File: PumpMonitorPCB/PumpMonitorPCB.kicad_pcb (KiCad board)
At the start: 2 copper layers, 51 parts, among them J3 Debug, J4 USB_C_Receptacle_USB2.0_16P, K1 J115F11CH5VDCS61-5U Relay, Q1 AS2302, U1 ACS770xCB-050B-PFF, U2 AMS1117-3.3, U3 ESP32-S3-WROOM-1, U4 MC14504B, U5 WIO-SX1262, U6 TPD3E001DRLR

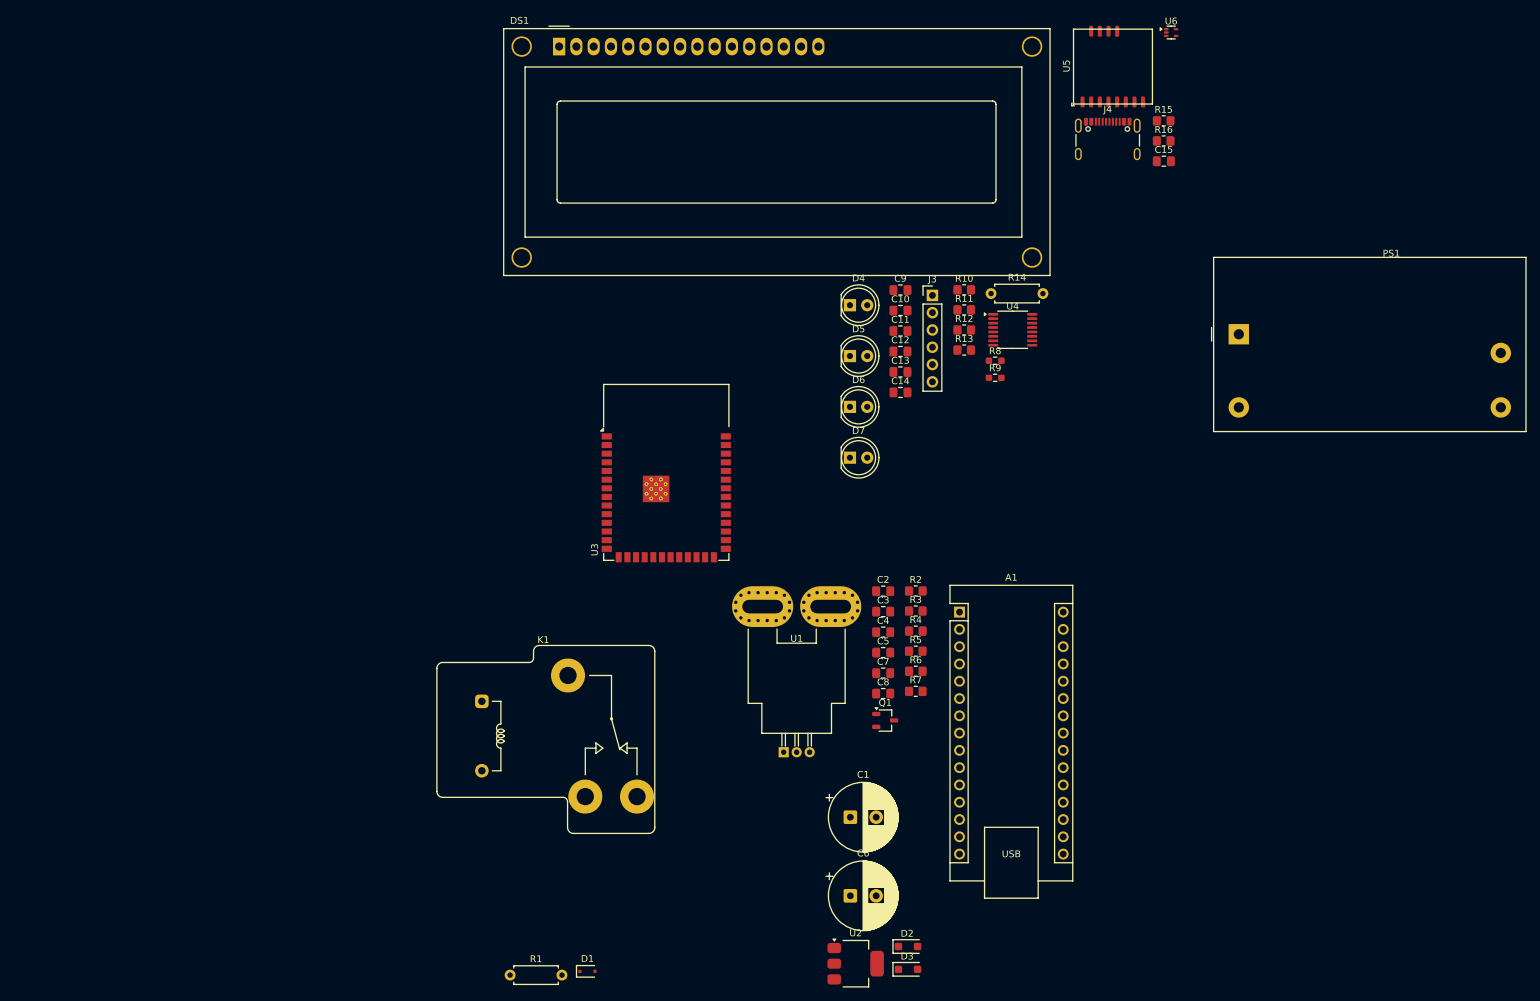
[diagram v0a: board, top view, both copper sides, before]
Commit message: Added op amps to voltage and current measurement, more footprint assignments.
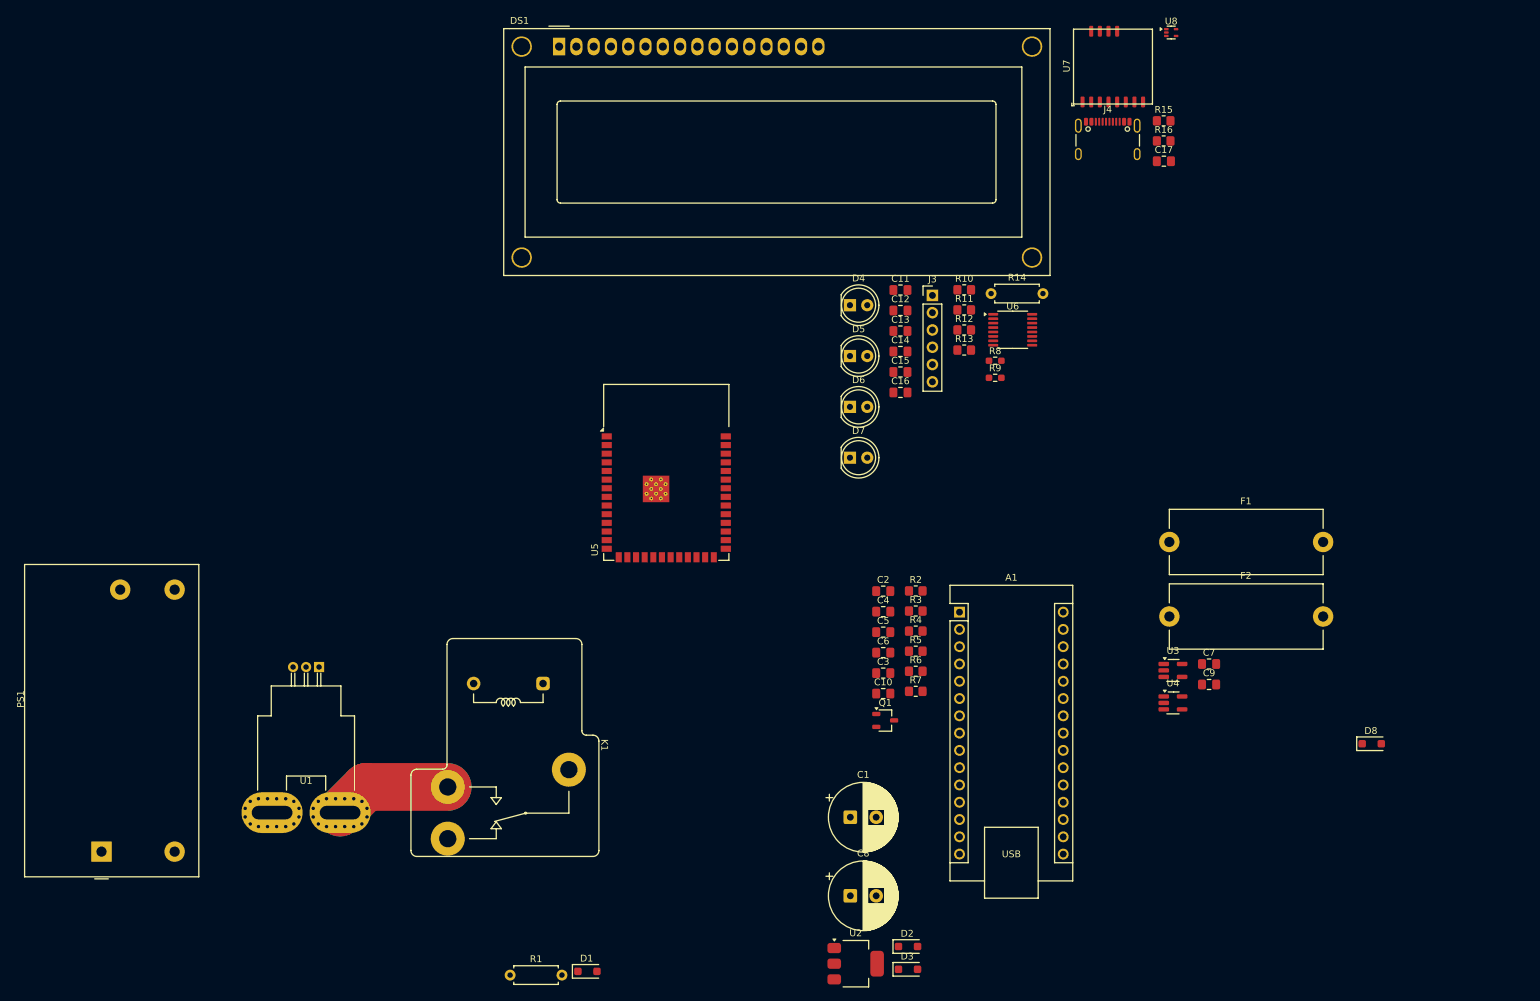
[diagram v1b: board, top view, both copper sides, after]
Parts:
- added C7: 100n, Capacitor_SMD:C_0805_2012Metric_Pad1.18x1.45mm_HandSolder, F.Cu at (194.3, 126.2)
- added C9: 100n, Capacitor_SMD:C_0805_2012Metric_Pad1.18x1.45mm_HandSolder, F.Cu at (194.3, 129.2)
- added D8: PMEG1020EH,115, Diode_SMD:D_SOD-123F, F.Cu at (218.2, 137.9)
- added F1: 600mA - 696103201002, Fuse:Fuseholder_Cylinder-5x20mm_Stelvio-Kontek_PTF78_Horizontal_Open, F.Cu at (188.4, 108.3)
- added F2: 600mA - 696103201002, Fuse:Fuseholder_Cylinder-5x20mm_Stelvio-Kontek_PTF78_Horizontal_Open, F.Cu at (188.4, 119.2)
- added U3: LMV321, Package_TO_SOT_SMD:SOT-23-5_HandSoldering, F.Cu at (189.0, 127.1)
- added U4: LMV321, Package_TO_SOT_SMD:SOT-23-5_HandSoldering, F.Cu at (189.0, 131.9)
- C12: renamed from C10; value 0.1u -> 100n
- C14: renamed from C12; value 0.1u -> 100n
- C15: renamed from C13; value 0.1u -> 100n
- C16: renamed from C14; value 0.1u -> 100n
- C17: renamed from C15; value 0.1u -> 100n
- C2: value C -> 47n
- C3: renamed from C7; value 0.1u -> 100n
- C4: renamed from C3; value 0.1u -> 100n
- C6: renamed from C5; value 0.1u -> 100n
- D1: value B5819WSL-TP -> PMEG1020EH,115; footprint Diode_SMD:D_SOD-323F -> Diode_SMD:D_SOD-123F
- moved PS1 183.6 mm to (31.5, 153.8), turned to 90 degrees
- moved U1 69.4 mm to (63.5, 126.6), turned to 180 degrees
- moved K1 13.8 mm to (100.2, 141.7), turned to -90 degrees
- renumbered C8 to C10, C9 to C11, C11 to C13, C4 to C5, C6 to C8, U3 to U5, U4 to U6, U5 to U7, U6 to U8
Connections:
- C2 pad 1: /Main PCB/Mains and power supply/Current measurement -> Net-(U3-+)
- C5 pad 1: /Main PCB/Mains and power supply/Voltage sense -> Net-(D2-K)
- D2 pad 1: /Main PCB/Mains and power supply/Voltage sense -> Net-(D2-K)
- J4 pad A4: +5V -> Net-(D8-A)
- J4 pad A9: +5V -> Net-(D8-A)
- J4 pad B4: +5V -> Net-(D8-A)
- J4 pad B9: +5V -> Net-(D8-A)
- R2 pad 2: /Main PCB/Mains and power supply/Current measurement -> Net-(U3-+)
- R3 pad 1: /Main PCB/Mains and power supply/Voltage sense -> Net-(D2-K)
- R4 pad 1: /Main PCB/Mains and power supply/Voltage sense -> Net-(D2-K)
- R5 pad 2: /Main PCB/Mains and power supply/Current measurement -> Net-(U3-+)
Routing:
- net Net-(U1-IP-): track 0.00 -> 34.8 mm

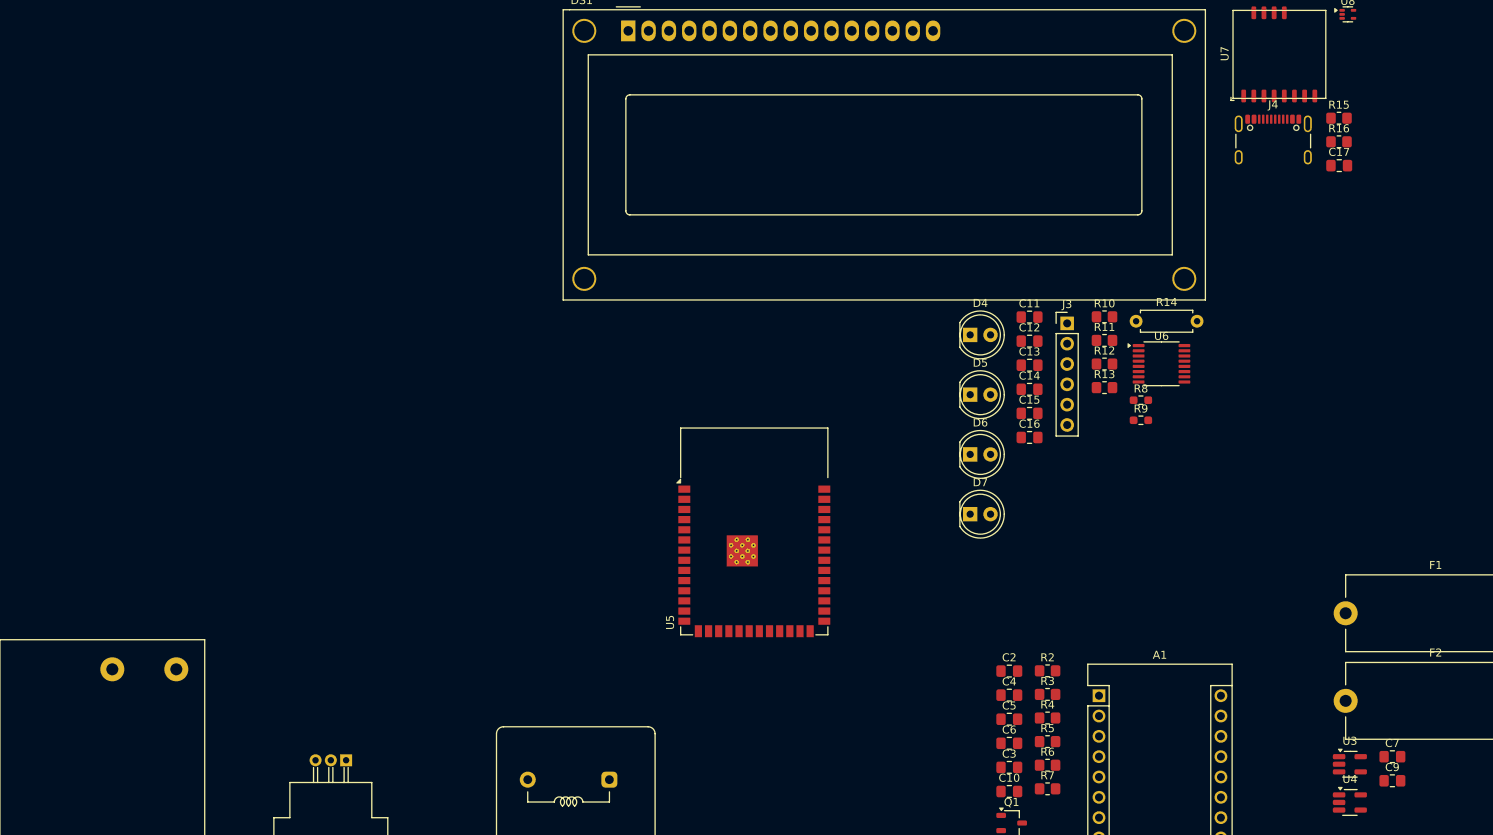
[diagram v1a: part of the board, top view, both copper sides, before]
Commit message: Added terminals footprint and 3D model.
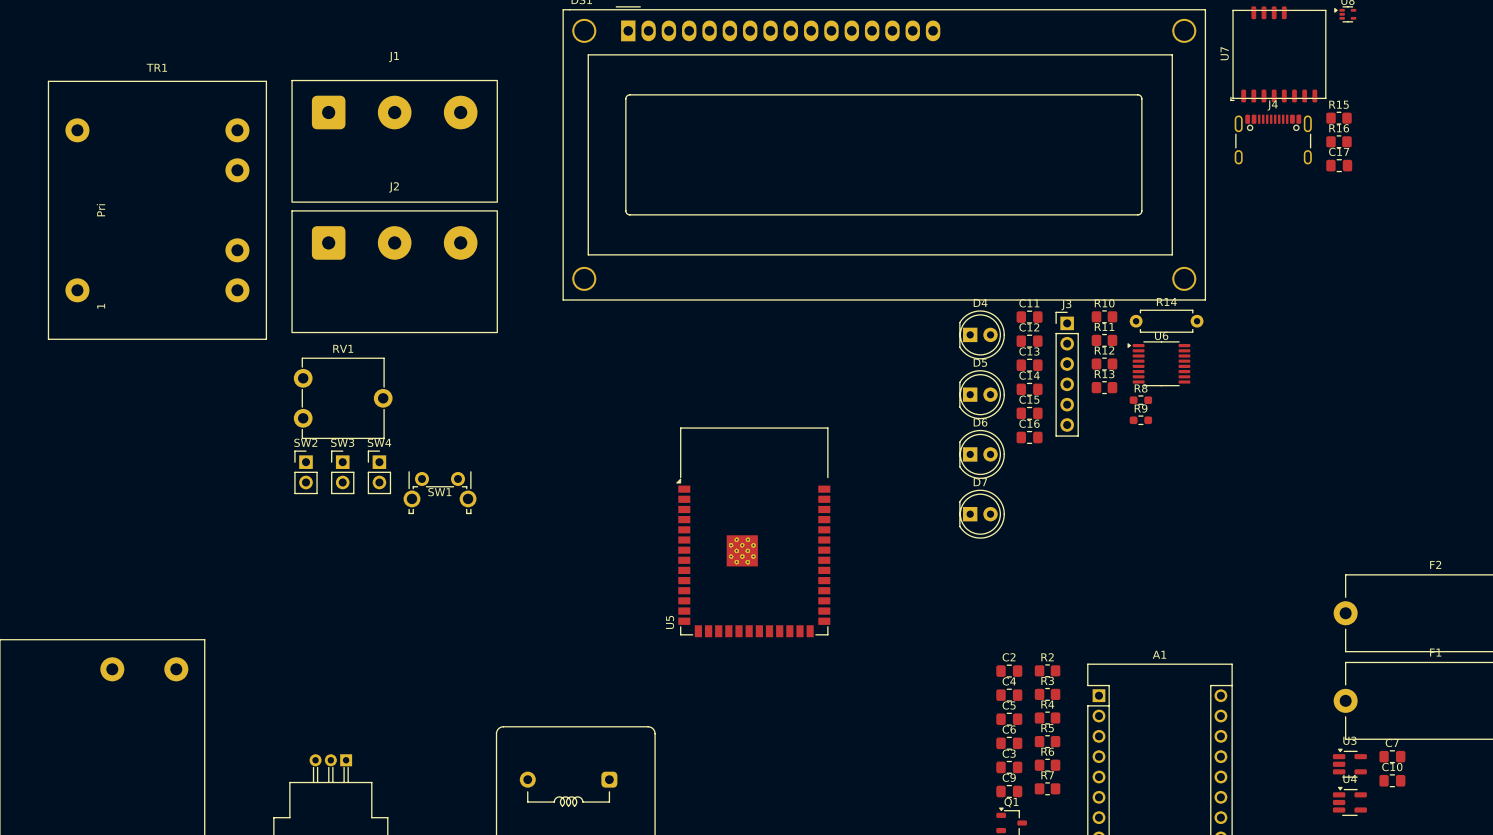
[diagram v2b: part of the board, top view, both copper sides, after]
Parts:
- added J1: Mains terminals, PumpMonitorCustomFootprints:8.25mm_ScrewTerminals, F.Cu at (69.6, 45.7)
- added J2: Mains terminals, PumpMonitorCustomFootprints:8.25mm_ScrewTerminals, F.Cu at (69.6, 62.0)
- added RV1: 10k, Potentiometer_THT:Potentiometer_ACP_CA9-V10_Vertical, F.Cu at (58.1, 83.9)
- added SW1: EN, Button_Switch_THT:SW_Tactile_SPST_Angled_PTS645Vx39-2LFS, F.Cu at (73.0, 91.5)
- added SW2: BOOT, Connector_PinHeader_2.54mm:PinHeader_1x02_P2.54mm_Vertical, F.Cu at (58.5, 89.4)
- added SW3: LEFT, Connector_PinHeader_2.54mm:PinHeader_1x02_P2.54mm_Vertical, F.Cu at (63.1, 89.4)
- added SW4: RIGHT, Connector_PinHeader_2.54mm:PinHeader_1x02_P2.54mm_Vertical, F.Cu at (67.7, 89.4)
- added TR1: BV302D06012, PumpMonitorCustomFootprints:Transformer_BV302D06012, F.Cu at (29.9, 67.9)
- K1: value J115F11CH5VDCS61-5U Relay -> J115F11CH5VDCS61-5U
- renumbered C9 to C10, C10 to C9, F2 to F1, F1 to F2
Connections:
- net /Main PCB/Live In renamed /Main PCB/Live in
- F2 pad 2: Net-(U1-IP+) -> Net-(F2-Pad2)
- K1 pad 14: Net-(U1-IP-) -> Net-(F2-Pad2)
- PS1 pad 1: /Main PCB/Neutral -> /Main PCB/Neutral in
- U1 pad 4: Net-(U1-IP+) -> /Main PCB/Neutral out
- U1 pad 5: Net-(U1-IP-) -> /Main PCB/Neutral in
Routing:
- net Net-(U1-IP-): track 34.8 -> 0.00 mm
- net (no net): track 0.00 -> 34.8 mm

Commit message: Rejigged auxilliary connectors, experimetning with kiclearance.
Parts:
- removed A1: Arduino_Nano_v3.x, Module:Arduino_Nano
- added C18: 100n, Capacitor_SMD:C_0603_1608Metric_Pad1.08x0.95mm_HandSolder, F.Cu at (223.5, 87.8)
- added C19: 100n, Capacitor_SMD:C_0603_1608Metric_Pad1.08x0.95mm_HandSolder, F.Cu at (245.8, 98.6)
- added C20: 100n, Capacitor_SMD:C_0603_1608Metric_Pad1.08x0.95mm_HandSolder, F.Cu at (245.8, 103.6)
- added C21: 100n, Capacitor_SMD:C_0603_1608Metric_Pad1.08x0.95mm_HandSolder, F.Cu at (241.3, 98.4)
- added C22: 100n, Capacitor_SMD:C_0603_1608Metric_Pad1.08x0.95mm_HandSolder, F.Cu at (245.8, 104.8)
- added D10: 3.3V - DDZ9684-7, Diode_SMD:D_SOD-123F, F.Cu at (228.6, 87.8)
- added D11: 3.3V - DDZ9684-7, Diode_SMD:D_SOD-123F, F.Cu at (250.9, 98.6)
- added D12: 3.3V - DDZ9684-7, Diode_SMD:D_SOD-123F, F.Cu at (250.9, 103.6)
- added D13: PMEG1020EH,115, Diode_SMD:D_SOD-123F, F.Cu at (256.5, 144.2)
- added D14: 3.3V - DDZ9684-7, Diode_SMD:D_SOD-123F, F.Cu at (254.9, 104.7)
- added D15: 3.3V - DDZ9684-7, Diode_SMD:D_SOD-123F, F.Cu at (250.9, 104.8)
- added D8: Aux relay, LED_THT:LED_D5.0mm, F.Cu at (276.9, 99.0)
- added J10: Aux GPIO 4, Connector_PinHeader_2.54mm:PinHeader_1x06_P2.54mm_Vertical, F.Cu at (251.5, 144.8)
- added J3: Mains terminals, PumpMonitorCustomFootprints:8.25mm_ScrewTerminals, F.Cu at (287.8, 65.2)
- added J4: Auxilliary relay, PumpMonitorCustomFootprints:8.25mm_ScrewTerminals, F.Cu at (287.8, 81.5)
- added J7: Aux GPIO 1, Connector_PinHeader_2.54mm:PinHeader_1x06_P2.54mm_Vertical, F.Cu at (237.7, 144.8)
- added J8: Aux GPIO 2, Connector_PinHeader_2.54mm:PinHeader_1x06_P2.54mm_Vertical, F.Cu at (242.3, 144.8)
- added J9: Aux GPIO 3, Connector_PinHeader_2.54mm:PinHeader_1x06_P2.54mm_Vertical, F.Cu at (246.9, 144.8)
- added K2: J115F11CH5VDCS61-5U, J115F11CH5VDCS61_5U_Relay:J115F11CH5VDCS61-5U, F.Cu at (255.3, 118.6)
- added Q2: AS2302, Package_TO_SOT_SMD:TSOT-23, F.Cu at (256.4, 148.3)
- added R15: 220, Resistor_SMD:R_0603_1608Metric_Pad0.98x0.95mm_HandSolder, F.Cu at (276.6, 104.0)
- added R19: 10k, Resistor_SMD:R_0603_1608Metric_Pad0.98x0.95mm_HandSolder, F.Cu at (223.5, 82.7)
- added R2: 10k, Resistor_SMD:R_0603_1608Metric_Pad0.98x0.95mm_HandSolder, F.Cu at (286.1, 96.5)
- added R20: 10k, Resistor_SMD:R_0603_1608Metric_Pad0.98x0.95mm_HandSolder, F.Cu at (226.1, 87.8)
- added R21: 10k, Resistor_SMD:R_0603_1608Metric_Pad0.98x0.95mm_HandSolder, F.Cu at (245.8, 93.5)
- added R22: 10k, Resistor_SMD:R_0603_1608Metric_Pad0.98x0.95mm_HandSolder, F.Cu at (248.4, 98.6)
- added R23: 10k, Resistor_SMD:R_0603_1608Metric_Pad0.98x0.95mm_HandSolder, F.Cu at (245.8, 98.5)
- added R24: 10k, Resistor_SMD:R_0603_1608Metric_Pad0.98x0.95mm_HandSolder, F.Cu at (248.4, 103.6)
- added R25: 5.6k, Resistor_SMD:R_0603_1608Metric_Pad0.98x0.95mm_HandSolder, F.Cu at (227.0, 82.7)
- added R26: 5.6k, Resistor_SMD:R_0603_1608Metric_Pad0.98x0.95mm_HandSolder, F.Cu at (249.3, 93.5)
- added R27: 5.6k, Resistor_SMD:R_0603_1608Metric_Pad0.98x0.95mm_HandSolder, F.Cu at (249.3, 98.5)
- added R28: 10k, Resistor_SMD:R_0603_1608Metric_Pad0.98x0.95mm_HandSolder, F.Cu at (245.6, 108.4)
- added R29: 10k, Resistor_SMD:R_0603_1608Metric_Pad0.98x0.95mm_HandSolder, F.Cu at (250.0, 90.9)
- added R30: 10k, Resistor_SMD:R_0603_1608Metric_Pad0.98x0.95mm_HandSolder, F.Cu at (245.8, 99.8)
- added R31: 10k, Resistor_SMD:R_0603_1608Metric_Pad0.98x0.95mm_HandSolder, F.Cu at (248.4, 104.8)
- added R32: 10k, Resistor_SMD:R_0603_1608Metric_Pad0.98x0.95mm_HandSolder, F.Cu at (255.9, 151.8)
- added R33: 5.6k, Resistor_SMD:R_0603_1608Metric_Pad0.98x0.95mm_HandSolder, F.Cu at (250.0, 93.4)
- added R34: 5.6k, Resistor_SMD:R_0603_1608Metric_Pad0.98x0.95mm_HandSolder, F.Cu at (249.3, 99.8)
- C10, C11, C12, C13, C14, C15, C16, C17, C2, C3, C4, C5, C6, C7, C9: footprint Capacitor_SMD:C_0805_2012Metric_Pad1.18x1.45mm_HandSolder -> Capacitor_SMD:C_0603_1608Metric_Pad1.08x0.95mm_HandSolder
- F1: renamed from F2; value 600mA - 696103201002 -> 600mA
- F2: renamed from F1; value 600mA - 696103201002 -> 600mA
- J1: value Mains terminals -> Live terminals
- J2: value Mains terminals -> Neutral terminals
- R1: footprint Resistor_THT:R_Axial_DIN0207_L6.3mm_D2.5mm_P7.62mm_Horizontal -> Resistor_THT:R_Axial_DIN0309_L9.0mm_D3.2mm_P12.70mm_Horizontal
- R10: footprint Resistor_SMD:R_0805_2012Metric_Pad1.20x1.40mm_HandSolder -> Resistor_SMD:R_0603_1608Metric_Pad0.98x0.95mm_HandSolder
- R12: renamed from R11; footprint Resistor_SMD:R_0805_2012Metric_Pad1.20x1.40mm_HandSolder -> Resistor_SMD:R_0603_1608Metric_Pad0.98x0.95mm_HandSolder
- R13: renamed from R12; footprint Resistor_SMD:R_0805_2012Metric_Pad1.20x1.40mm_HandSolder -> Resistor_SMD:R_0603_1608Metric_Pad0.98x0.95mm_HandSolder
- R14: renamed from R13; footprint Resistor_SMD:R_0805_2012Metric_Pad1.20x1.40mm_HandSolder -> Resistor_SMD:R_0603_1608Metric_Pad0.98x0.95mm_HandSolder
- R16: renamed from R14; footprint Resistor_THT:R_Axial_DIN0207_L6.3mm_D2.5mm_P7.62mm_Horizontal -> Resistor_THT:R_Axial_DIN0309_L9.0mm_D3.2mm_P12.70mm_Horizontal
- R17: renamed from R15; footprint Resistor_SMD:R_0805_2012Metric_Pad1.20x1.40mm_HandSolder -> Resistor_SMD:R_0603_1608Metric_Pad0.98x0.95mm_HandSolder
- R18: renamed from R16; footprint Resistor_SMD:R_0805_2012Metric_Pad1.20x1.40mm_HandSolder -> Resistor_SMD:R_0603_1608Metric_Pad0.98x0.95mm_HandSolder
- R3: renamed from R2; footprint Resistor_SMD:R_0805_2012Metric_Pad1.20x1.40mm_HandSolder -> Resistor_SMD:R_0603_1608Metric_Pad0.98x0.95mm_HandSolder
- R4: renamed from R3; footprint Resistor_SMD:R_0805_2012Metric_Pad1.20x1.40mm_HandSolder -> Resistor_SMD:R_0603_1608Metric_Pad0.98x0.95mm_HandSolder
- R5: renamed from R4; footprint Resistor_SMD:R_0805_2012Metric_Pad1.20x1.40mm_HandSolder -> Resistor_SMD:R_0603_1608Metric_Pad0.98x0.95mm_HandSolder
- R6: renamed from R5; footprint Resistor_SMD:R_0805_2012Metric_Pad1.20x1.40mm_HandSolder -> Resistor_SMD:R_0603_1608Metric_Pad0.98x0.95mm_HandSolder
- R7: renamed from R6; footprint Resistor_SMD:R_0805_2012Metric_Pad1.20x1.40mm_HandSolder -> Resistor_SMD:R_0603_1608Metric_Pad0.98x0.95mm_HandSolder
- R8: renamed from R7; footprint Resistor_SMD:R_0805_2012Metric_Pad1.20x1.40mm_HandSolder -> Resistor_SMD:R_0603_1608Metric_Pad0.98x0.95mm_HandSolder
- moved C10 205.0 mm to (-8.48, 99.1)
- moved C7 205.0 mm to (-8.48, 96.0)
- moved U3 205.0 mm to (-13.8, 97.0)
- moved U4 205.0 mm to (-13.8, 101.8)
- moved F2 201.3 mm to (-2.54, 182.9), turned to 90 degrees
- moved F1 193.3 mm to (10.2, 182.9), turned to 90 degrees
- moved J1 139.0 mm to (34.9, 180.3)
- moved R1 134.2 mm to (-33.0, 121.9)
- moved J2 118.6 mm to (61.6, 180.3)
- moved Q1 116.2 mm to (30.5, 134.5)
- moved U5 107.8 mm to (16.4, 53.5)
- moved SW4 104.6 mm to (163.1, 86.4)
- moved SW1 104.6 mm to (177.6, 88.5)
- moved RV1 104.6 mm to (162.7, 80.9)
- moved SW2 104.6 mm to (167.6, 86.4)
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- renumbered D8 to D9, J3 to J5, J4 to J6, R9 to R11, R8 to R9, SW3 to SW2, SW4 to SW3, SW2 to SW4
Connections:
- J1 pad 2: /Main PCB/Live out -> /Main PCB/Live in
- J1 pad 3: /Main PCB/Neutral in -> /Main PCB/Live out
- J2 pad 1: /Main PCB/Neutral out -> /Main PCB/Neutral in
- J2 pad 2: Earth_Protective -> /Main PCB/Neutral in
- J2 pad 3: Earth_Protective -> /Main PCB/Neutral out
- J5 pad 6: /Main PCB/Microcontroller and UI/BOOT -> /Main PCB/Microcontroller and UI/BOOT/OK
- U5 pad 17: /Main PCB/Auxilliary connectors/Aux.9 -> /Main PCB/Auxilliary connectors/Aux.relay
- U5 pad 23: /Main PCB/Microcontroller and UI/LORA.DIO0 -> /Main PCB/Auxilliary connectors/LORA.DIO1
- U5 pad 7: /Main PCB/Auxilliary connectors/Aux.6 -> /Main PCB/Auxilliary connectors/Aux.7
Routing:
- net /Main PCB/Neutral in: track 0.00 -> 190.4 mm
- net Net-(PS1-AC/L): track 0.00 -> 58.5 mm
- net /Main PCB/Live in: track 0.00 -> 47.8 mm
- net /Main PCB/Live out: track 0.00 -> 45.3 mm
- net (no net): track 34.8 -> 0.00 mm
- net Net-(F1-Pad2): track 0.00 -> 27.0 mm
- net /Main PCB/Neutral out: track 0.00 -> 23.2 mm
- net Earth: track 0.00 -> 16.5 mm
